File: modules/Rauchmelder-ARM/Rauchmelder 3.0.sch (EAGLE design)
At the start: 61 parts, among them IC2 LPC1115, IC3 BD9G101, Q1 BC856, Q3 BCP52, Q4 ASFL, T1 BC848

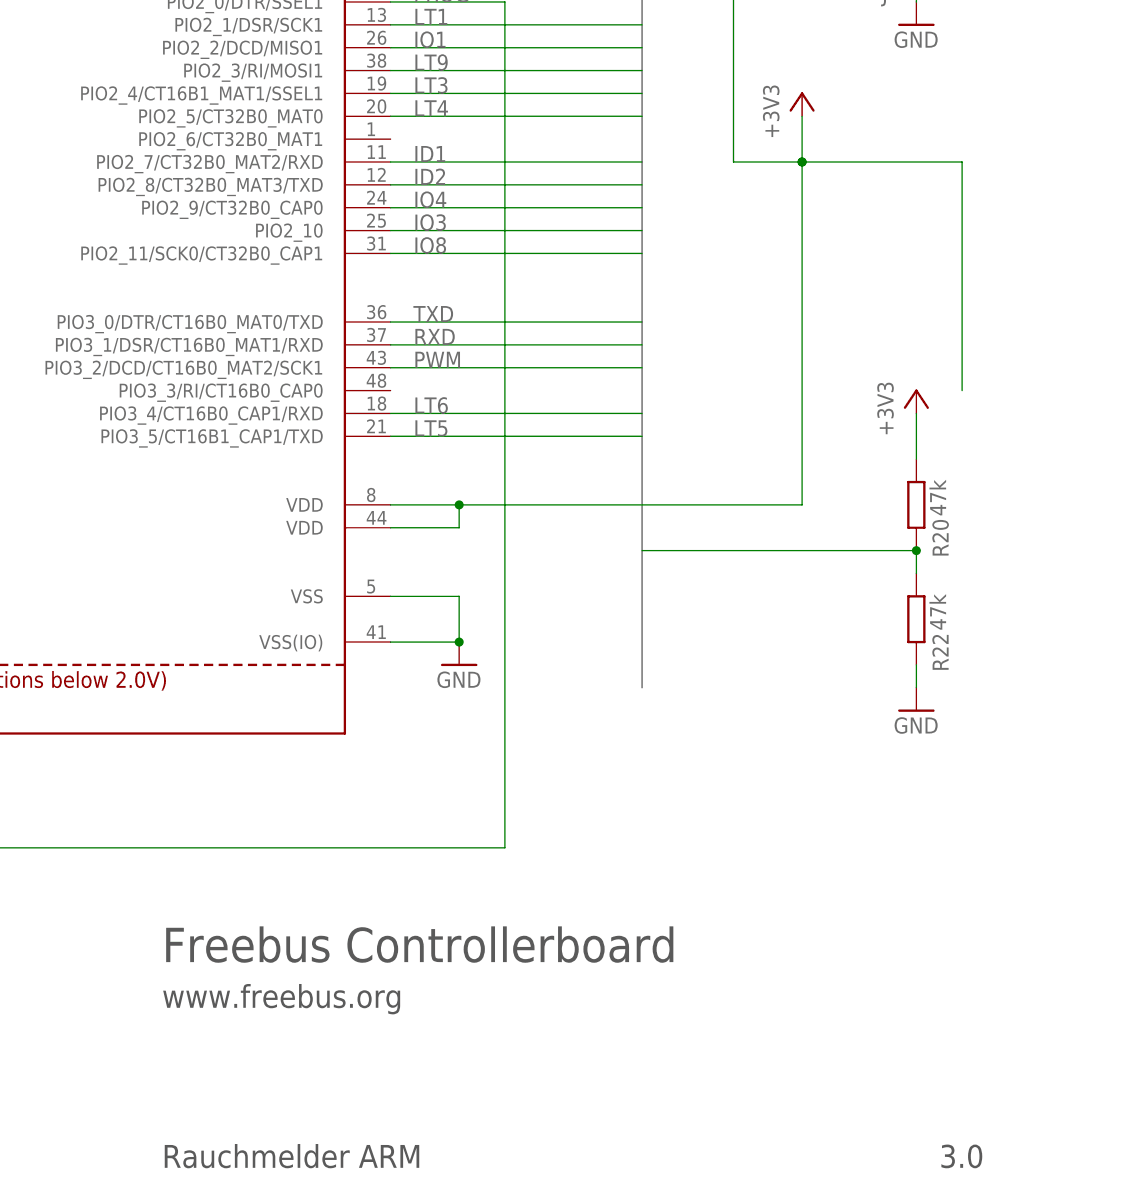
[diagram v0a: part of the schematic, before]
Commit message: Beschriftungen geändert
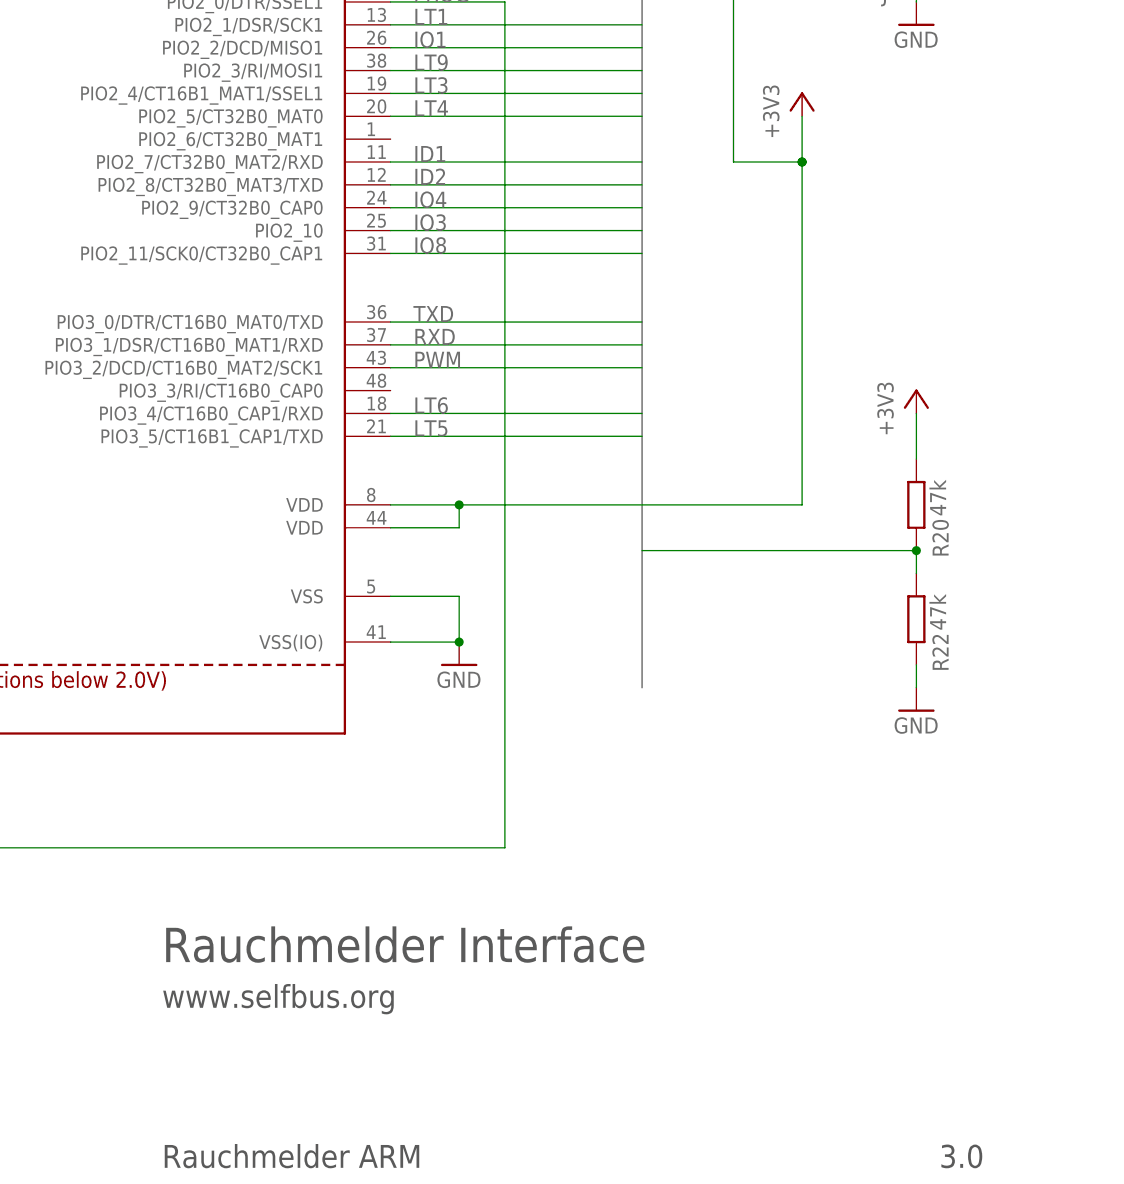
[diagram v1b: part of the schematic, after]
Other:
- note added: "Rauchmelder Interface"
- note added: "www.selfbus.org"
- note removed: "Freebus Controllerboard"
- note removed: "www.freebus.org"
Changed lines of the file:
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@@
 <grid distance="0.1" unitdist="inch" unit="inch" style="lines" multiple="1" display="no" altdistance="0.01" altunitdist="inch" altunit="inch"/>
 <layers>
-<layer number="1" name="Top" color="4" fill="1" visible="yes" active="no"/>
-<layer number="2" name="Route2" color="1" fill="3" visible="yes" active="no"/>
-<layer number="3" name="Route3" color="4" fill="3" visible="yes" active="no"/>
-<layer number="4" name="Route4" color="1" fill="4" visible="yes" active="no"/>
-<layer number="5" name="Route5" color="4" fill="4" visible="yes" active="no"/>
-<layer number="6" name="Route6" color="1" fill="8" visible="yes" active="no"/>
-<layer number="7" name="Route7" color="4" fill="8" visible="yes" active="no"/>
-<layer number="8" name="Route8" color="1" fill="2" visible="yes" active="no"/>
-<layer number="9" name="Route9" color="4" fill="2" visible="yes" active="no"/>
-<layer number="10" name="Route10" color="1" fill="7" visible="yes" active="no"/>
-<layer number="11" name="Route11" color="4" fill="7" visible="yes" active="no"/>
-<layer number="12" name="Route12" color="1" fill="5" visible="yes" active="no"/>
-<layer number="13" name="Route13" color="4" fill="5" visible="yes" active="no"/>
-<layer number="14" name="Route14" color="1" fill="6" visible="yes" active="no"/>
-<layer number="15" name="Route15" color="4" fill="6" visible="yes" active="no"/>
-<layer number="16" name="Bottom" color="1" fill="1" visible="yes" active="no"/>
-<layer number="17" name="Pads" color="2" fill="1" visible="yes" active="no"/>
-<layer number="18" name="Vias" color="2" fill="1" visible="yes" active="no"/>
-<layer number="19" name="Unrouted" color="6" fill="1" visible="yes" active="no"/>
-<layer number="20" name="Dimension" color="15" fill="1" visible="yes" active="no"/>
-<layer number="21" name="tPlace" color="7" fill="1" visible="yes" active="no"/>
-<layer number="22" name="bPlace" color="7" fill="1" visible="yes" active="no"/>
-<layer number="23" name="tOrigins" color="15" fill="1" visible="yes" active="no"/>
-<layer number="24" name="bOrigins" color="15" fill="1" visible="yes" active="no"/>
-<layer number="25" name="tNames" color="7" fill="1" visible="yes" active="no"/>
-<layer number="26" name="bNames" color="7" fill="1" visible="yes" active="no"/>
-<layer number="27" name="tValues" color="7" fill="1" visible="yes" active="no"/>
-<layer number="28" name="bValues" color="7" fill="1" visible="yes" active="no"/>
+<layer number="1" name="Top" color="4" fill="1" visible="no" active="no"/>
+<layer number="2" name="Route2" color="1" fill="3" visible="no" active="no"/>
+<layer number="3" name="Route3" color="4" fill="3" visible="no" active="no"/>
+<layer number="4" name="Route4" color="1" fill="4" visible="no" active="no"/>
+<layer number="5" name="Route5" color="4" fill="4" visible="no" active="no"/>
+<layer number="6" name="Route6" color="1" fill="8" visible="no" active="no"/>
+<layer number="7" name="Route7" color="4" fill="8" visible="no" active="no"/>
+<layer number="8" name="Route8" color="1" fill="2" visible="no" active="no"/>
+<layer number="9" name="Route9" color="4" fill="2" visible="no" active="no"/>
+<layer number="10" name="Route10" color="1" fill="7" visible="no" active="no"/>
+<layer number="11" name="Route11" color="4" fill="7" visible="no" active="no"/>
+<layer number="12" name="Route12" color="1" fill="5" visible="no" active="no"/>
+<layer number="13" name="Route13" color="4" fill="5" visible="no" active="no"/>
+<layer number="14" name="Route14" color="1" fill="6" visible="no" active="no"/>
+<layer number="15" name="Route15" color="4" fill="6" visible="no" active="no"/>
+<layer number="16" name="Bottom" color="1" fill="1" visible="no" active="no"/>
+<layer number="17" name="Pads" color="2" fill="1" visible="no" active="no"/>
+<layer number="18" name="Vias" color="2" fill="1" visible="no" active="no"/>
+<layer number="19" name="Unrouted" color="6" fill="1" visible="no" active="no"/>
+<layer number="20" name="Dimension" color="15" fill="1" visible="no" active="no"/>
+<layer number="21" name="tPlace" color="7" fill="1" visible="no" active="no"/>
+<layer number="22" name="bPlace" color="7" fill="1" visible="no" active="no"/>
+<layer number="23" name="tOrigins" color="15" fill="1" visible="no" active="no"/>
+<layer number="24" name="bOrigins" color="15" fill="1" visible="no" active="no"/>
+<layer number="25" name="tNames" color="7" fill="1" visible="no" active="no"/>
+<layer number="26" name="bNames" color="7" fill="1" visible="no" active="no"/>
+<layer number="27" name="tValues" color="7" fill="1" visible="no" active="no"/>
+<layer number="28" name="bValues" color="7" fill="1" visible="no" active="no"/>
 <layer number="29" name="tStop" color="7" fill="3" visible="no" active="no"/>
 <layer number="30" name="bStop" color="7" fill="6" visible="no" active="no"/>
@@
 <layer number="35" name="tGlue" color="7" fill="4" visible="no" active="no"/>
 <layer number="36" name="bGlue" color="7" fill="5" visible="no" active="no"/>
-<layer number="37" name="tTest" color="7" fill="1" visible="yes" active="no"/>
-<layer number="38" name="bTest" color="7" fill="1" visible="yes" active="no"/>
+<layer number="37" name="tTest" color="7" fill="1" visible="no" active="no"/>
+<layer number="38" name="bTest" color="7" fill="1" visible="no" active="no"/>
 <layer number="39" name="tKeepout" color="4" fill="11" visible="no" active="no"/>
 <layer number="40" name="bKeepout" color="1" fill="11" visible="no" active="no"/>
@@
 <layer number="44" name="Drills" color="7" fill="1" visible="no" active="no"/>
 <layer number="45" name="Holes" color="7" fill="1" visible="no" active="no"/>
-<layer number="46" name="Milling" color="3" fill="1" visible="yes" active="no"/>
-<layer number="47" name="Measures" color="7" fill="1" visible="yes" active="no"/>
-<layer number="48" name="Document" color="7" fill="1" visible="yes" active="no"/>
-<layer number="49" name="Reference" color="7" fill="1" visible="yes" active="no"/>
-<layer number="50" name="dxf" color="7" fill="1" visible="yes" active="no"/>
-<layer number="51" name="tDocu" color="7" fill="1" visible="yes" active="no"/>
-<layer number="52" name="bDocu" color="7" fill="1" visible="yes" active="no"/>
-<layer number="53" name="tGND_GNDA" color="7" fill="9" visible="yes" active="no"/>
-<layer number="54" name="bGND_GNDA" color="1" fill="9" visible="yes" active="no"/>
-<layer number="56" name="wert" color="7" fill="1" visible="yes" active="no"/>
+<layer number="46" name="Milling" color="3" fill="1" visible="no" active="no"/>
+<layer number="47" name="Measures" color="7" fill="1" visible="no" active="no"/>
+<layer number="48" name="Document" color="7" fill="1" visible="no" active="no"/>
+<layer number="49" name="Reference" color="7" fill="1" visible="no" active="no"/>
+<layer number="50" name="dxf" color="7" fill="1" visible="no" active="no"/>
+<layer number="51" name="tDocu" color="7" fill="1" visible="no" active="no"/>
+<layer number="52" name="bDocu" color="7" fill="1" visible="no" active="no"/>
+<layer number="53" name="tGND_GNDA" color="7" fill="9" visible="no" active="no"/>
+<layer number="54" name="bGND_GNDA" color="1" fill="9" visible="no" active="no"/>
+<layer number="56" name="wert" color="7" fill="1" visible="no" active="no"/>
 <layer number="91" name="Nets" color="2" fill="1" visible="yes" active="yes"/>
 <layer number="92" name="Busses" color="1" fill="1" visible="yes" active="yes"/>
@@
 <text x="10.16" y="86.36" size="1.778" layer="95">Bus +</text>
 <text x="10.16" y="73.66" size="1.778" layer="95">GND</text>
-<text x="317.5" y="33.02" size="3.81" layer="97">Freebus Controllerboard</text>
-<text x="317.5" y="27.94" size="2.54" layer="97">www.freebus.org</text>
+<text x="317.5" y="33.02" size="3.81" layer="97">Rauchmelder Interface</text>
+<text x="317.5" y="27.94" size="2.54" layer="97">www.selfbus.org</text>
 <text x="317.5" y="10.16" size="2.54" layer="97">Rauchmelder ARM</text>
 <text x="403.86" y="10.16" size="2.54" layer="97">3.0</text>
@@
 <segment>
 <wire x1="388.62" y1="127" x2="388.62" y2="121.92" width="0.1524" layer="91"/>
-<wire x1="388.62" y1="121.92" x2="406.4" y2="121.92" width="0.1524" layer="91"/>
 <pinref part="P+6" gate="G$1" pin="+3V3"/>
 <pinref part="IC2" gate="G$1" pin="VDD@1"/>
@@
 <wire x1="381" y1="121.92" x2="388.62" y2="121.92" width="0.1524" layer="91"/>
 <junction x="388.62" y="121.92"/>
-<wire x1="406.4" y1="121.92" x2="406.4" y2="96.52" width="0.1524" layer="91"/>
-</segment>
-<segment>
+</segment>
+<segment>
